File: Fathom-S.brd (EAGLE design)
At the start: 112.4 x 45.7 mm, 111 parts, among them IC1 LMH6643, IC2 LMH6643, IC3 ST490AB, IC4 ST490AB, IC5 FT230XS, Q1 BC817-40W, U1 MC7812, U2 MC7805, U4 INA139, U5 MC7805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

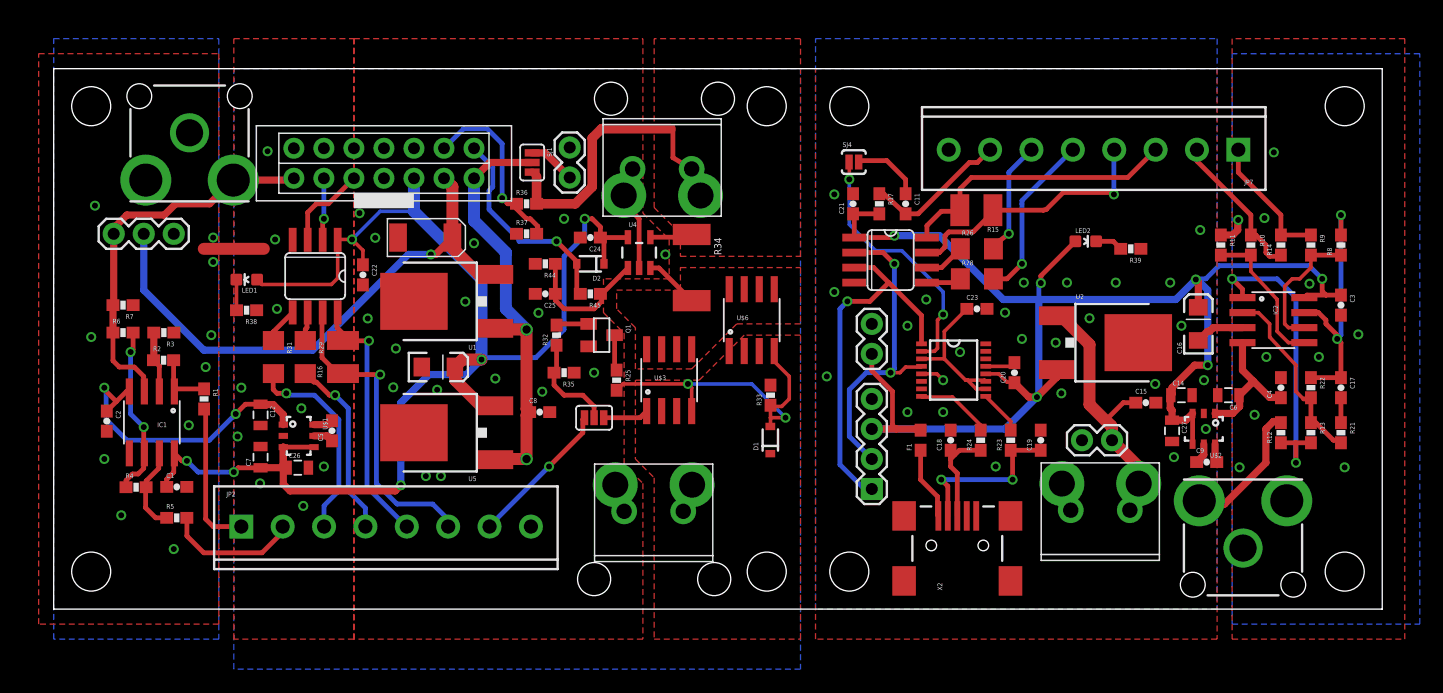
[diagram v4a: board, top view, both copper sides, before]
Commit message: Fixed a bunch of routing issues, added more ground vias, changed ground planes a bit.
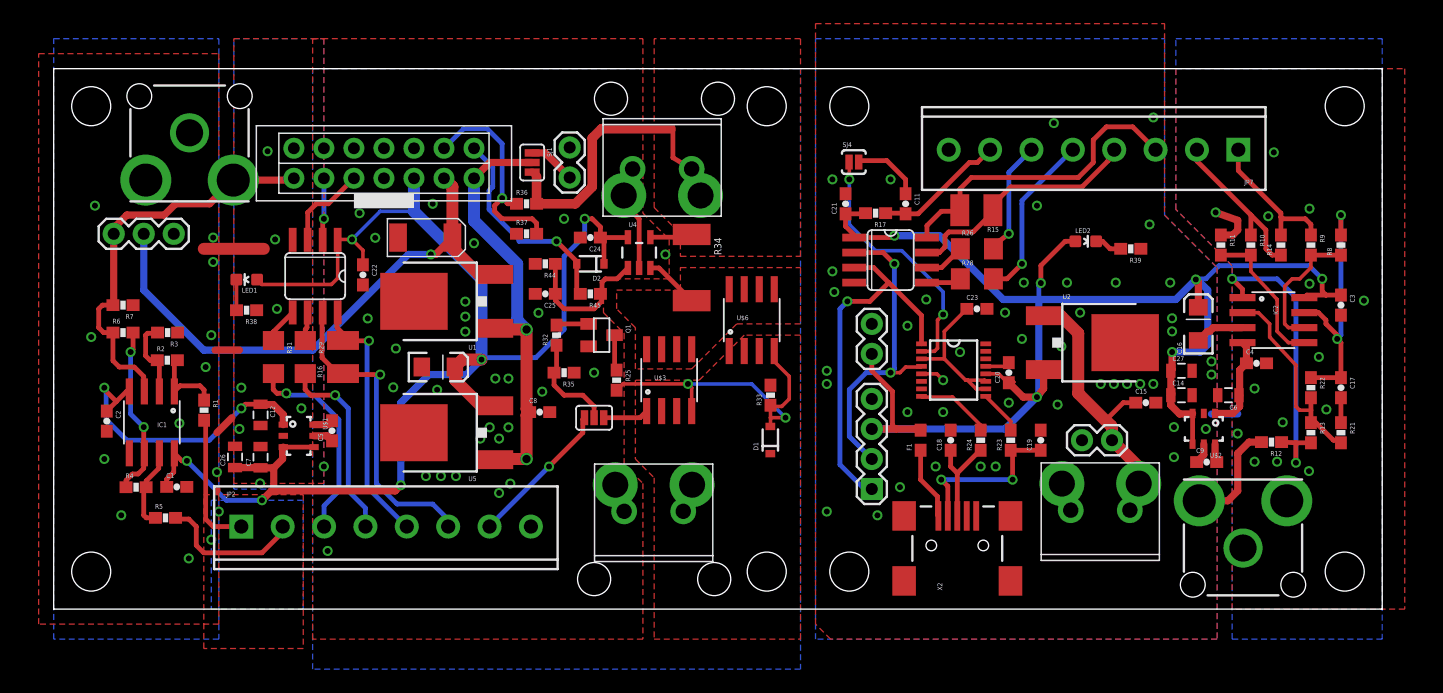
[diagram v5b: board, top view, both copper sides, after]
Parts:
- moved C26 5.39 mm to (15.3, 12.9), turned to 90 degrees
- moved C27 5.14 mm to (95.4, 20.2), turned to 0 degrees
- moved C4 2.92 mm to (101.8, 20.8), turned to 0 degrees
- moved R12 1.12 mm to (103.0, 14.1), turned to 180 degrees
- moved U2 1.11 mm to (89.1, 22.5)
- moved R1 0.95 mm to (12.7, 16.8)
- moved R5 0.95 mm to (9.46, 7.72)
- moved R17 0.85 mm to (69.5, 33.5), turned to 180 degrees
- moved C21 0.63 mm to (67.0, 34.3)
- moved C20 0.48 mm to (80.8, 20.0)
- moved R3 0.32 mm to (9.64, 23.4)
- moved R2 0.32 mm to (9.61, 21.1)
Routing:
- net GND: track 11.3 -> 15.3 mm, vias 35 -> 58
- net GND-ISO: track 9.69 -> 13.7 mm, vias 35 -> 49
- net -VCC: track 11.8 -> 8.18 mm
- net VCC-ISO: track 118.2 -> 121.2 mm
- net VIDEO-OUT: track 12.2 -> 9.18 mm
- net V_SENSE: track 15.7 -> 18.4 mm
- net TOP-TP2+: track 25.3 -> 28.0 mm
- net TOP-TP2-: track 23.3 -> 21.1 mm, vias 1 -> 0
- net CAMERA: track 32.8 -> 34.7 mm
- net N$5: track 5.19 -> 6.70 mm
- net N$15: track 16.2 -> 17.5 mm
- net N$1: track 5.27 -> 6.47 mm
- net TOP-TP1-: track 12.8 -> 14.0 mm
- net ROV-ON-CTRL: track 12.3 -> 11.1 mm
- net TOP-TP1+: track 11.2 -> 12.4 mm
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
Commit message: Changed the op-amp package because the MSOPs are much cheaper for some reason.
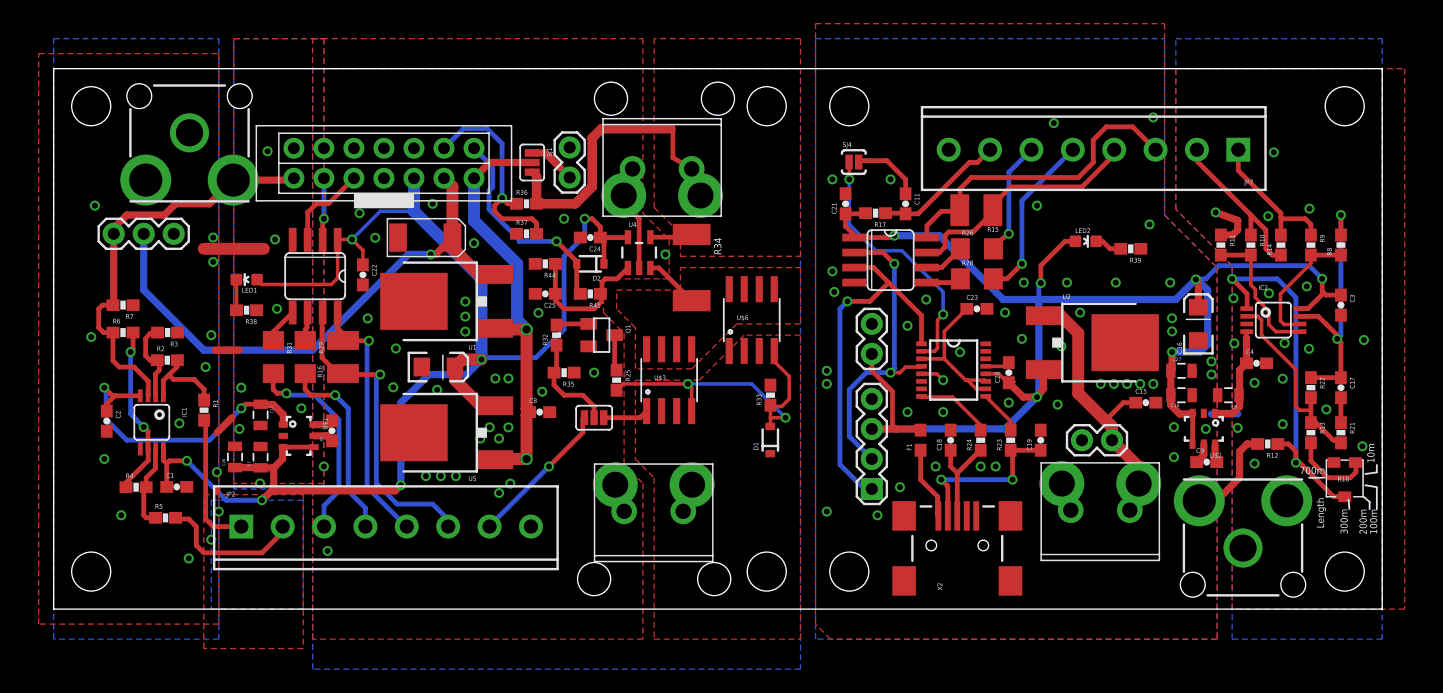
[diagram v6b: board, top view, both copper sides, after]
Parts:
- added R18: TC33X-2-102E, SparkFun-Electromechanical:TRIMPOT_TC33
- IC1, IC2: device SparkFun-AnalogIC:SO08 -> BlueRobotics-Main:MSOP8
- R13: value 3.6K -> 1.5K
- moved R12 0.35 mm to (102.7, 14.0)
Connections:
- new net N$12: R13.2, R18.1
- net N$17: now also R18.2; no longer R13.2
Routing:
- net N$12: track 0.00 -> 6.96 mm
- net N$17: track 26.2 -> 31.1 mm
- net GND: track 15.3 -> 11.1 mm, vias 58 -> 62
- net N$1: track 6.47 -> 8.25 mm
- net VIDEO-OUT: track 9.18 -> 8.24 mm
- net -VCC-ISO: track 25.1 -> 26.0 mm
- net -VCC: track 8.18 -> 8.99 mm
- net VCC-ISO: track 121.2 -> 121.9 mm
- net N$15: track 17.5 -> 16.8 mm
- net VCC: track 123.7 -> 124.4 mm
- net N$8: track 12.6 -> 11.9 mm
- net CAMERA: track 34.7 -> 35.3 mm
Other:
- board text added: "100m"
- board text added: "10m"
- board text added: "200m"
- board text added: "300m"
- board text added: "700m"
- board text added: "Length"
- board text removed: "VIDEO OUT"

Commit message: Minor changes to readme and silkscreen.
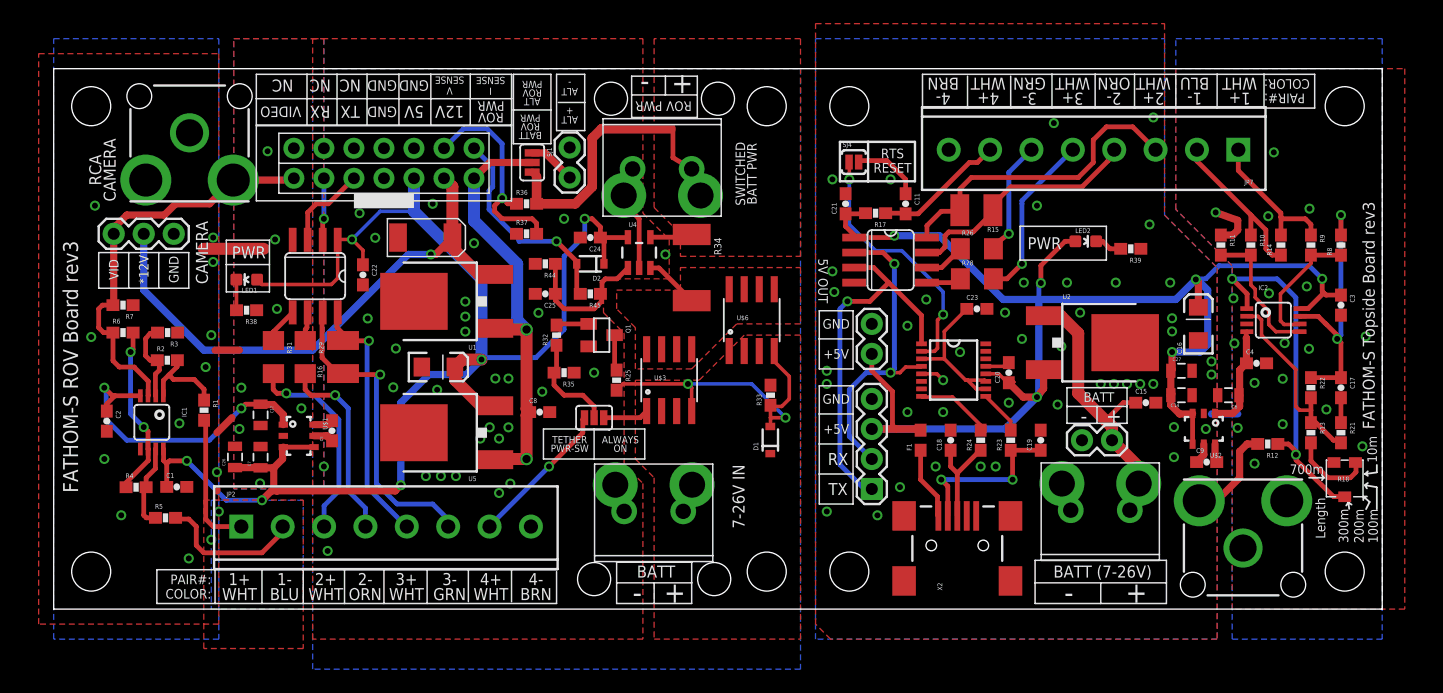
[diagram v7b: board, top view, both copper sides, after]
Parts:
- U$4, U$7: device BR-Eagle-Library:BR-FULL-LOGO-MEDIUM -> BlueRobotics-Main:BR-FULL-LOGO-MEDIUM
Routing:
- net N$17: track 31.1 -> 30.3 mm

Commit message: Yet more layout changes and added ferrite beads to the -5V outputs for better noise rejection.
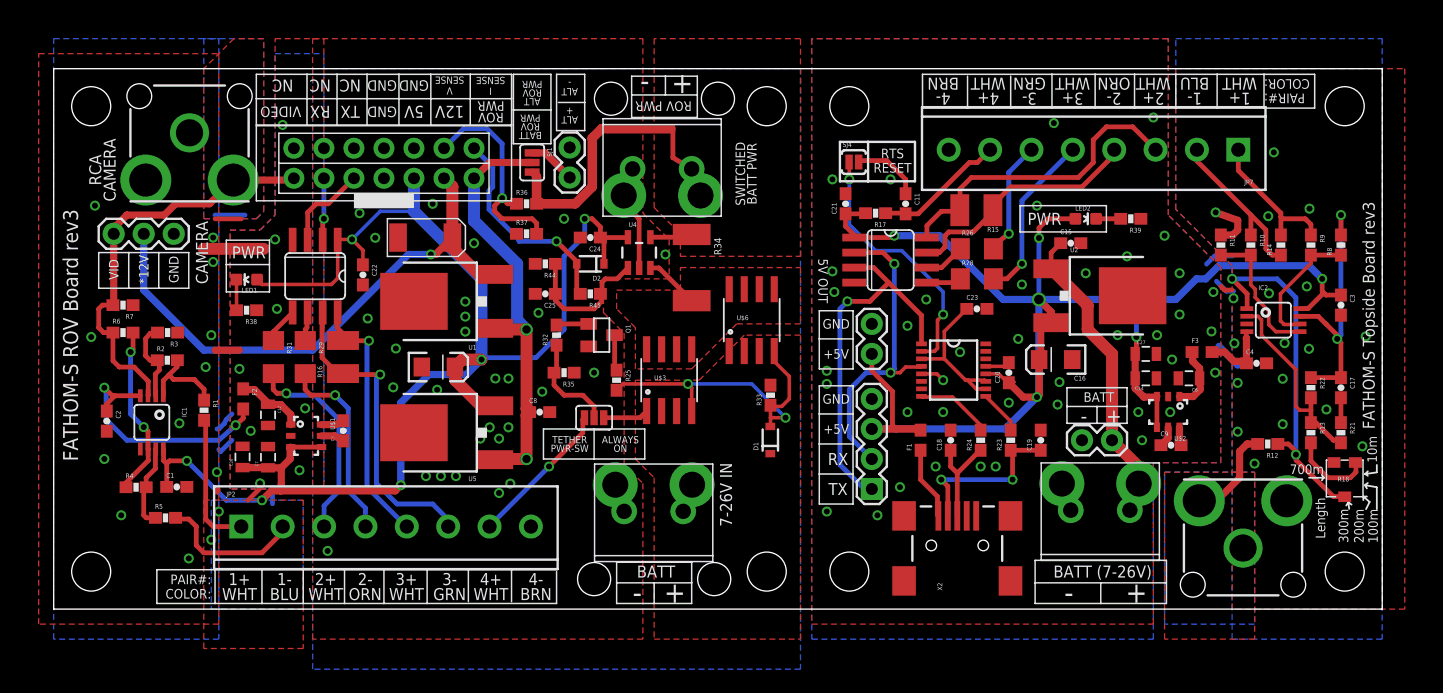
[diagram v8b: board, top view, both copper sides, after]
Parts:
- added F2, F3: 500mA, SparkFun:0603
- U$5: value LOGOBR-LOGO-MS -> LOGOBR-LOGO-MS-COPPER; device BR-Eagle-Library:BR-LOGO-MEDIUM-SMALL -> BlueRobotics-Main:BR-LOGO-MEDIUM-SMALL-COPPER
- U$9: device BR-Eagle-Library:BR-LOGO-MEDIUM-SMALL -> BlueRobotics-Main:BR-LOGO-MEDIUM-SMALL-COPPER
- moved U$9 58.7 mm to (5.10, 6.45), turned to 90 degrees
- moved C15 14.9 mm to (86.0, 31.0)
- moved C16 12.4 mm to (84.8, 21.1), turned to 180 degrees
- moved U$5 6.92 mm to (110.3, 34.3), turned to 90 degrees
- moved U2 4.02 mm to (89.7, 26.5)
- moved C6 3.63 mm to (96.0, 19.5)
- moved C14 3.34 mm to (92.4, 19.5)
- moved C27 3.34 mm to (92.4, 21.6)
- moved U$2 3.34 mm to (94.3, 16.7)
- moved C9 3.34 mm to (94.5, 13.9)
- moved R39 2.54 mm to (91.1, 33.0)
- moved LED2 1.91 mm to (87.3, 33.0)
- moved C5 0.95 mm to (24.5, 15.1)
- moved C12 0.64 mm to (18.1, 16.4)
- moved C7 0.64 mm to (18.1, 12.9)
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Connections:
- new net -VCC-ISO-PRE: C12.1, F2.1, U$1.1
- new net -VCC-PRE: C6.1, F3.1, U$2.1
- net -VCC: now also F3.2; no longer C6.1, U$2.1
- net -VCC-ISO: now also F2.2; no longer C12.1, U$1.1
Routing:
- net GND-ISO: track 13.7 -> 23.2 mm
- net -VCC-ISO-PRE: track 0.00 -> 5.83 mm
- net -VCC-PRE: track 0.00 -> 5.47 mm
- net GND: track 11.1 -> 16.6 mm, vias 62 -> 58
- net -VCC-ISO: track 26.0 -> 21.6 mm
- net -VCC: track 8.99 -> 6.08 mm
- net TOP-VIN: track 24.8 -> 26.3 mm
- net VCC: track 124.4 -> 125.1 mm
